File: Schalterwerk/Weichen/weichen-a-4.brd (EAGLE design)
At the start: 58.4 x 80 mm, 50 parts, among them Q1 P-MOSFET, Q2 P-MOSFET, X1 PHNX_4P_508CONN_1017493, X2 IO-HAT, X3 PHNX_4P_350CONN_1984989_PXC, X4 PHNX_4P_350CONN_1984989_PXC, X5 RJ45-JACK

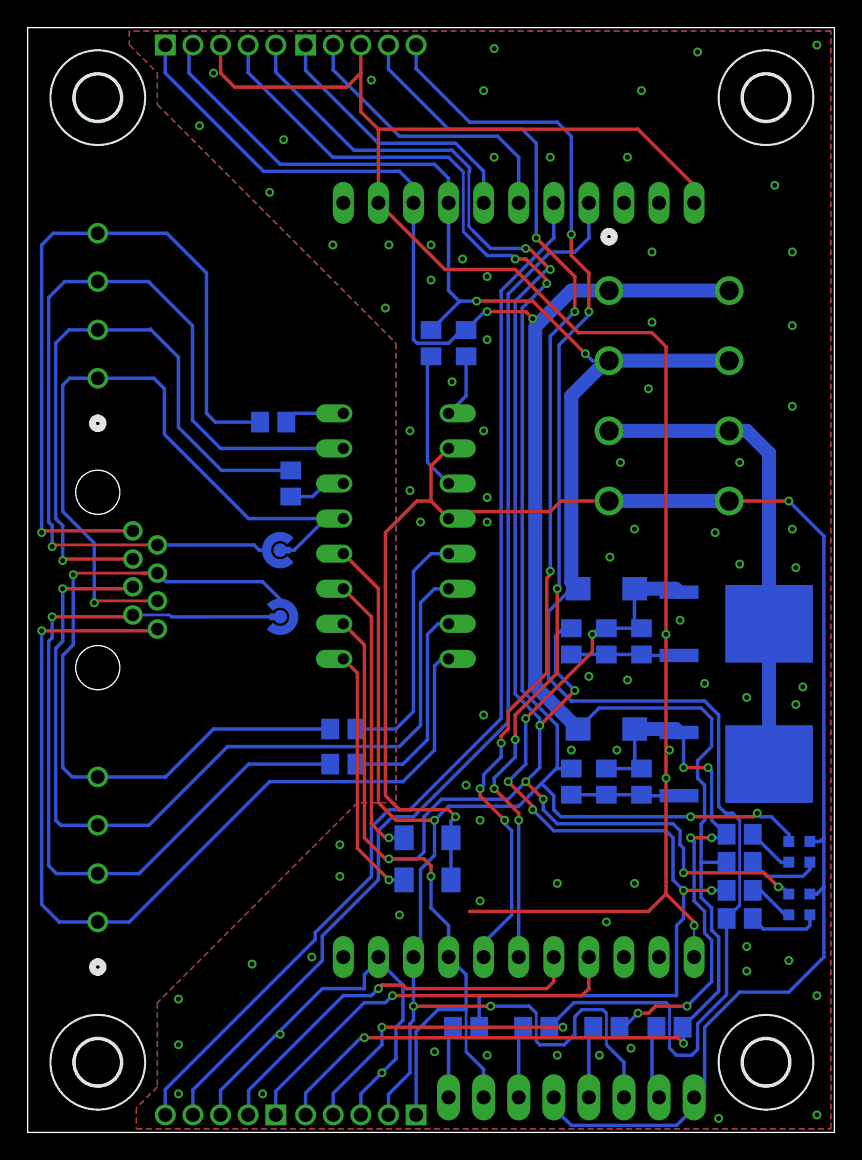
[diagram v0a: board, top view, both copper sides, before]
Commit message: Fixes issues found on the gerbers.
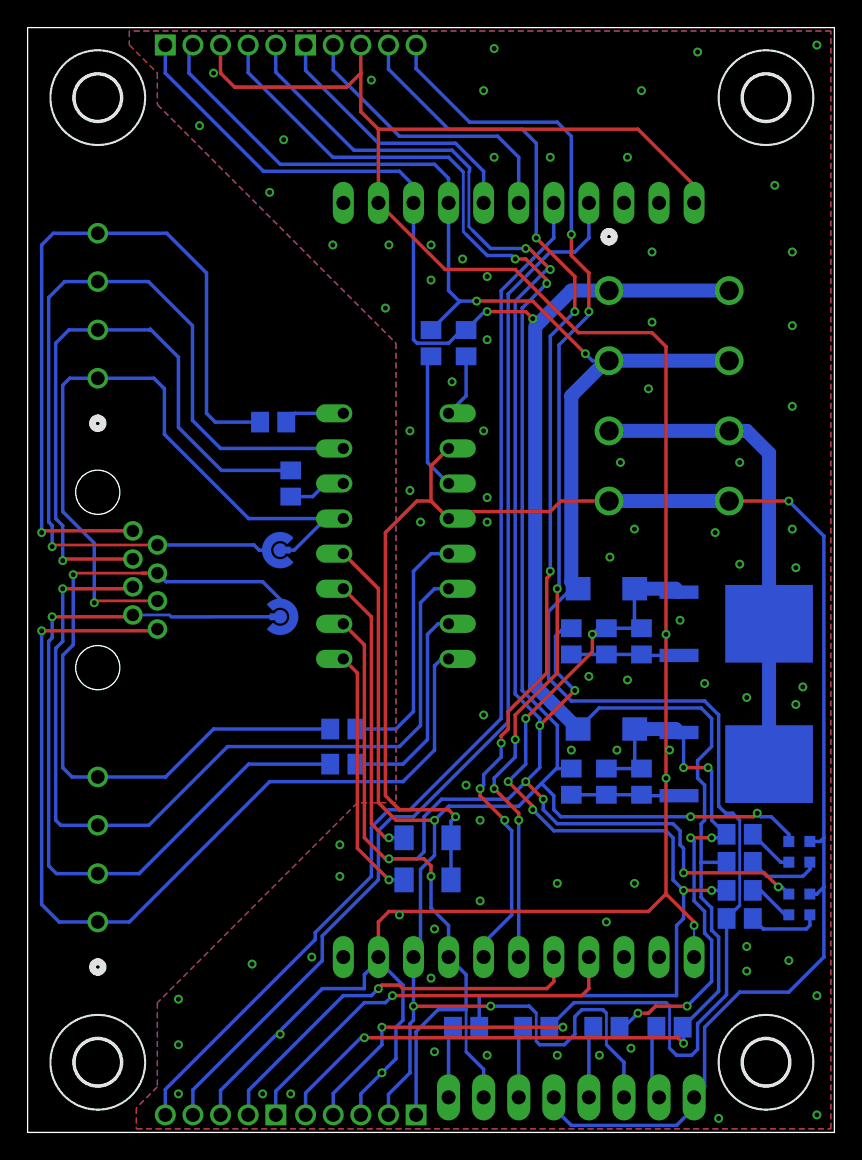
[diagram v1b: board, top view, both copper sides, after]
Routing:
- net GND: track 166.9 -> 176.3 mm, vias 85 -> 88
- net NX44: track 53.5 -> 52.9 mm
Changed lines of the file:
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@@
 <text x="20.066" y="56.388" size="1.016" layer="26" font="vector" ratio="10" rot="MR0">gn/w|</text>
 <text x="20.066" y="53.848" size="1.016" layer="26" font="vector" ratio="10" rot="MR0">gn|</text>
-<text x="20.066" y="24.384" size="1.016" layer="26" font="vector" ratio="10" rot="MR0">bl|</text>
-<text x="20.066" y="21.59" size="1.016" layer="26" font="vector" ratio="10" rot="MR0">bl/w|</text>
-<text x="20.066" y="17.526" size="1.016" layer="26" font="vector" ratio="10" rot="MR0">br/w|</text>
-<text x="20.066" y="14.732" size="1.016" layer="26" font="vector" ratio="10" rot="MR0">br|</text>
+<text x="20.066" y="25.4" size="1.016" layer="26" font="vector" ratio="10" rot="MR0">bl|</text>
+<text x="20.066" y="22.606" size="1.016" layer="26" font="vector" ratio="10" rot="MR0">bl/w|</text>
+<text x="20.066" y="18.542" size="1.016" layer="26" font="vector" ratio="10" rot="MR0">br/w|</text>
+<text x="20.066" y="15.748" size="1.016" layer="26" font="vector" ratio="10" rot="MR0">br|</text>
 <wire x1="18.288" y1="69.342" x2="18.288" y2="68.326" width="0.1524" layer="22"/>
 <wire x1="18.288" y1="68.326" x2="19.558" y2="67.056" width="0.1524" layer="22"/>
@@
 <wire x1="16.83" y1="51.435" x2="13.589" y2="51.435" width="0.254" layer="16"/>
 <wire x1="13.589" y1="51.435" x2="12.954" y2="52.07" width="0.254" layer="16"/>
-<wire x1="7.619996875" y1="43.56" x2="7.62" y2="43.56" width="0" layer="19" extent="16-16"/>
-<wire x1="1.016" y1="43.434" x2="1.016003125" y2="43.434" width="0" layer="19" extent="16-16"/>
+<wire x1="7.619996875" y1="43.56" x2="7.62" y2="43.56" width="0" layer="19" extent="1-1"/>
+<wire x1="1.016" y1="43.434" x2="1.016003125" y2="43.434" width="0" layer="19" extent="1-1"/>
 </signal>
 <signal name="NX42">
@@
 <wire x1="16.388" y1="42.54" x2="16.764" y2="42.164" width="0.254" layer="16"/>
 <wire x1="16.764" y1="42.164" x2="17.272" y2="42.164" width="0.254" layer="16"/>
-<wire x1="9.400003125" y1="42.54" x2="9.4" y2="42.54" width="0" layer="19" extent="1-1"/>
+<wire x1="9.4" y1="42.54" x2="9.400003125" y2="42.54" width="0" layer="19" extent="16-16"/>
 </signal>
 <signal name="NX43">
@@
 <wire x1="3.4166" y1="40.5006" x2="8.284325" y2="40.5006" width="0.2032" layer="1"/>
 <wire x1="3.4166" y1="40.5006" x2="3.302" y2="40.386" width="0.254" layer="1"/>
-<wire x1="5.08" y1="25.74" x2="5.674" y2="25.74" width="0.254" layer="16"/>
 <wire x1="8.284325" y1="40.5006" x2="9.3994" y2="40.5006" width="0.254" layer="1"/>
 <wire x1="9.3994" y1="40.5006" x2="9.4" y2="40.5" width="0.254" layer="1"/>
@@
 <contactref element="R2" pad="2"/>
 <contactref element="R4" pad="1"/>
-<wire x1="41.98" y1="34.54" x2="41.91" y2="34.61" width="0.254" layer="16"/>
 <wire x1="41.91" y1="34.61" x2="39.37" y2="34.61" width="0.254" layer="16"/>
 <contactref element="C2" pad="2"/>
@@
 <wire x1="36.7538" y1="32.3162" x2="36.7538" y2="58.3438" width="1.016" layer="16"/>
 <wire x1="50.8" y1="60.96" x2="42.1" y2="60.96" width="1.016" layer="16"/>
-<wire x1="36.51" y1="58.1" x2="36.7538" y2="58.3438" width="0.254" layer="16"/>
 <wire x1="36.7538" y1="58.3438" x2="36.83" y2="58.42" width="0.254" layer="16"/>
 <wire x1="31.75" y1="58.1" x2="31.43" y2="58.1" width="0.254" layer="16"/>
@@
 <wire x1="49.53" y1="14.647334375" x2="49.53" y2="16.256" width="0.254" layer="16"/>
 <wire x1="49.53" y1="16.256" x2="48.768" y2="17.018" width="0.254" layer="16"/>
-<wire x1="50.292" y1="19.304" x2="50.292" y2="19.238" width="0.254" layer="16"/>
 <wire x1="48.514" y1="25.654" x2="49.022" y2="25.146" width="0.254" layer="16"/>
 <wire x1="49.022" y1="25.146" x2="49.022" y2="22.606" width="0.254" layer="16"/>
@@
 <wire x1="29.464" y1="27.686" x2="29.464" y2="33.782" width="0.254" layer="16"/>
 <wire x1="29.464" y1="33.782" x2="29.972" y2="34.29" width="0.254" layer="16"/>
-<wire x1="1.016003125" y1="36.322" x2="1.016" y2="36.322" width="0" layer="19" extent="1-1"/>
-<wire x1="5.08" y1="15.24" x2="5.079996875" y2="15.24" width="0" layer="19" extent="1-1"/>
+<wire x1="1.016003125" y1="36.322" x2="1.016" y2="36.322" width="0" layer="19" extent="16-16"/>
+<wire x1="5.08" y1="15.24" x2="5.079996875" y2="15.24" width="0" layer="19" extent="16-16"/>
 </signal>
 <signal name="+12V">
@@
 <wire x1="46.228" y1="17.272" x2="48.26" y2="15.24" width="0.254" layer="1"/>
 <wire x1="46.228" y1="17.272" x2="44.958" y2="16.002" width="0.254" layer="1"/>
-<wire x1="44.958" y1="16.002" x2="32.004" y2="16.002" width="0.254" layer="1"/>
 <polygon width="0.0762" layer="16" spacing="0.254" isolate="0.254">
 <vertex x="58.166" y="79.756"/>
@@
 <via x="33.782" y="70.612" extent="1-16" drill="0.35"/>
 <via x="37.846" y="70.612" extent="1-16" drill="0.35"/>
+<via x="29.464" y="14.732" extent="1-16" drill="0.35"/>
+<via x="29.21" y="11.176" extent="1-16" drill="0.35"/>
+<wire x1="25.4" y1="15.24" x2="25.4" y2="12.7" width="0.254" layer="1"/>
+<wire x1="44.958" y1="16.002" x2="26.162" y2="16.002" width="0.254" layer="1"/>
+<wire x1="26.162" y1="16.002" x2="25.4" y2="15.24" width="0.254" layer="1"/>
+<via x="19.05" y="2.794" extent="1-16" drill="0.35"/>
 </signal>
 <signal name="OUT2">
@@
 <contactref element="R1" pad="2"/>
 <contactref element="C1" pad="2"/>
-<wire x1="47.168" y1="24.38" x2="47.098" y2="24.45" width="0.254" layer="16"/>
 <wire x1="39.37" y1="24.45" x2="41.91" y2="24.45" width="0.254" layer="16"/>
 <wire x1="41.91" y1="24.45" x2="44.45" y2="24.45" width="0.254" layer="16"/>
@@
 <wire x1="31.5468" y1="65.2272" x2="31.75" y2="65.024" width="0.2032" layer="16"/>
 <wire x1="31.5468" y1="69.5452" x2="31.5468" y2="65.2272" width="0.2032" layer="16"/>
-<wire x1="33.528003125" y1="9.144" x2="33.528" y2="9.144" width="0" layer="19" extent="1-1"/>
+<wire x1="33.528" y1="9.144" x2="33.528003125" y2="9.144" width="0" layer="19" extent="16-16"/>
 </signal>
 <signal name="IST2">
@@
 <via x="25.4" y="10.414" extent="1-16" drill="0.35"/>
 <wire x1="25.4" y1="10.414" x2="25.654" y2="10.668" width="0.254" layer="1"/>
-<wire x1="25.654" y1="10.668" x2="27.178" y2="10.668" width="0.254" layer="1"/>
-<wire x1="27.178" y1="10.668" x2="27.432" y2="10.414" width="0.254" layer="1"/>
-<wire x1="27.432" y1="10.414" x2="37.592" y2="10.414" width="0.254" layer="1"/>
+<wire x1="25.654" y1="10.668" x2="26.924" y2="10.668" width="0.254" layer="1"/>
+<wire x1="26.924" y1="10.668" x2="27.178" y2="10.414" width="0.254" layer="1"/>
+<wire x1="27.178" y1="10.414" x2="37.592" y2="10.414" width="0.254" layer="1"/>
 <wire x1="37.592" y1="10.414" x2="38.1" y2="10.922" width="0.254" layer="1"/>
 <wire x1="38.1" y1="10.922" x2="38.1" y2="12.7" width="0.254" layer="1"/>
